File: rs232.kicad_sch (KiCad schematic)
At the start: 7 parts, among them U7 SP3223

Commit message: wen branch and pr
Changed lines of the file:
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@@
 		(company "Hoppen")
+	)
+	(bus_alias "RS232_IN"
+		(members "RS232_IN_T" "RS232_IN_R")
+	)
+	(bus_alias "VN_RS232"
+		(members "RS232_OUT_T" "RS232_OUT_R")
 	)
 	(rectangle
@@
 		)
 	)
-	(hierarchical_label "{RS232_OUT}"
+	(hierarchical_label "{VN_RS232}"
 		(shape input)
 		(at 182.88 107.95 0)

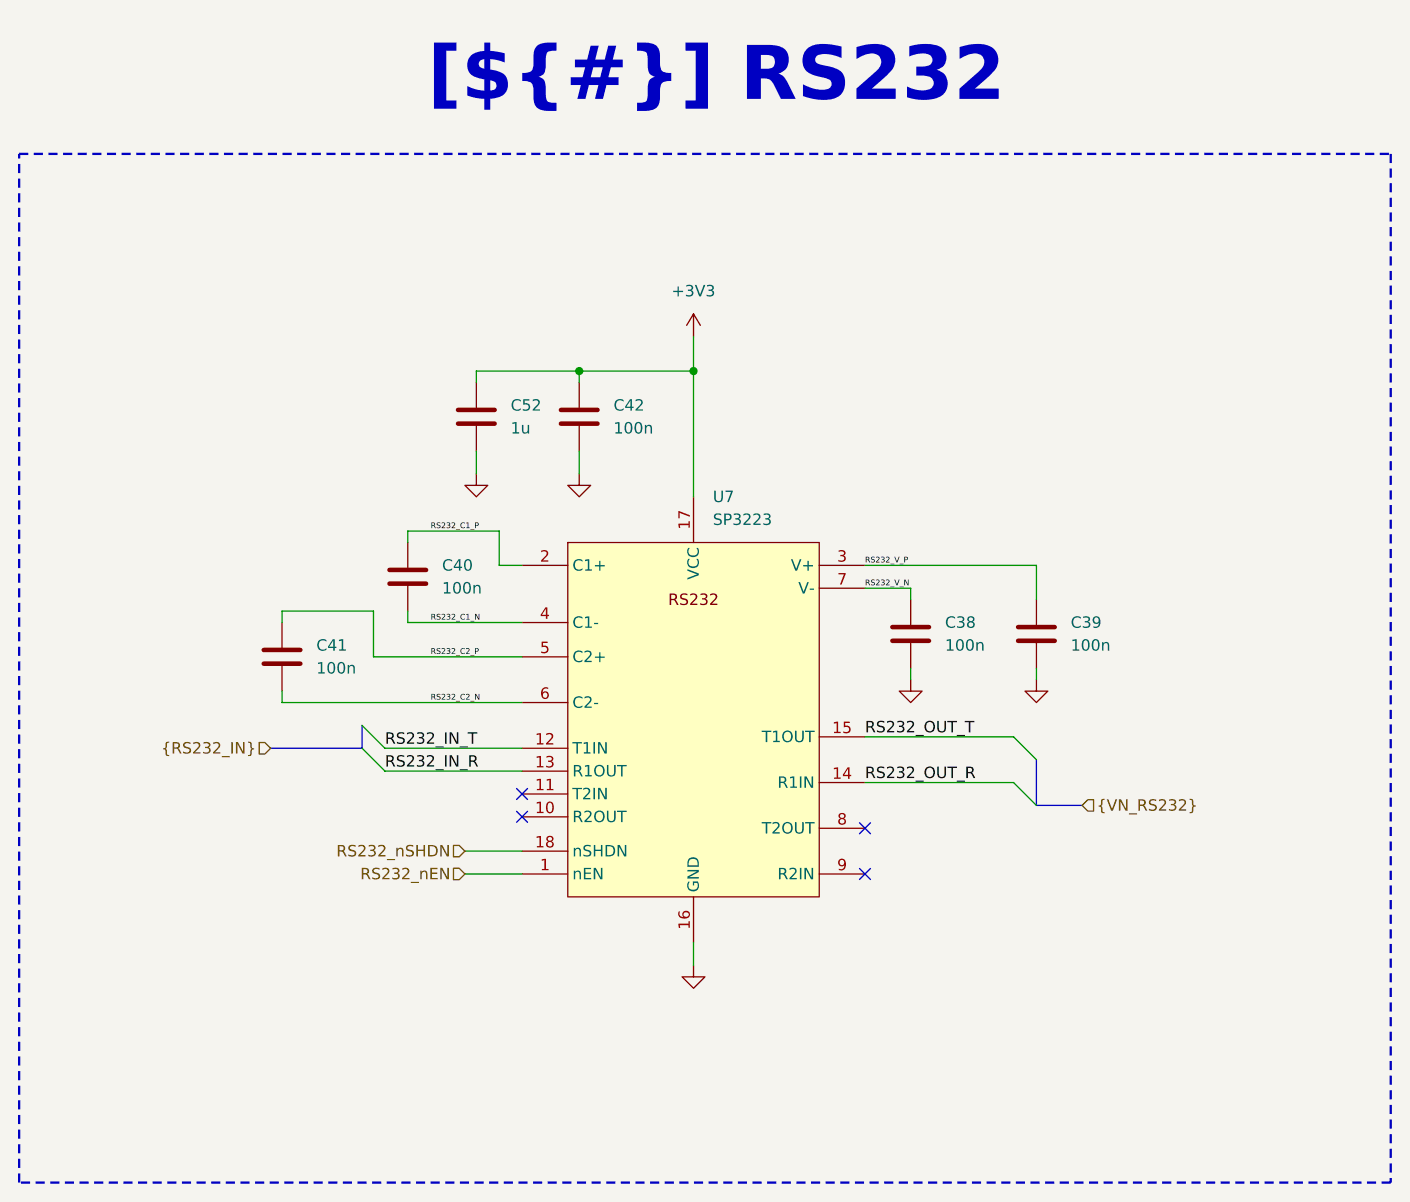
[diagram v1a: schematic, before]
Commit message: much work and .ioc file added
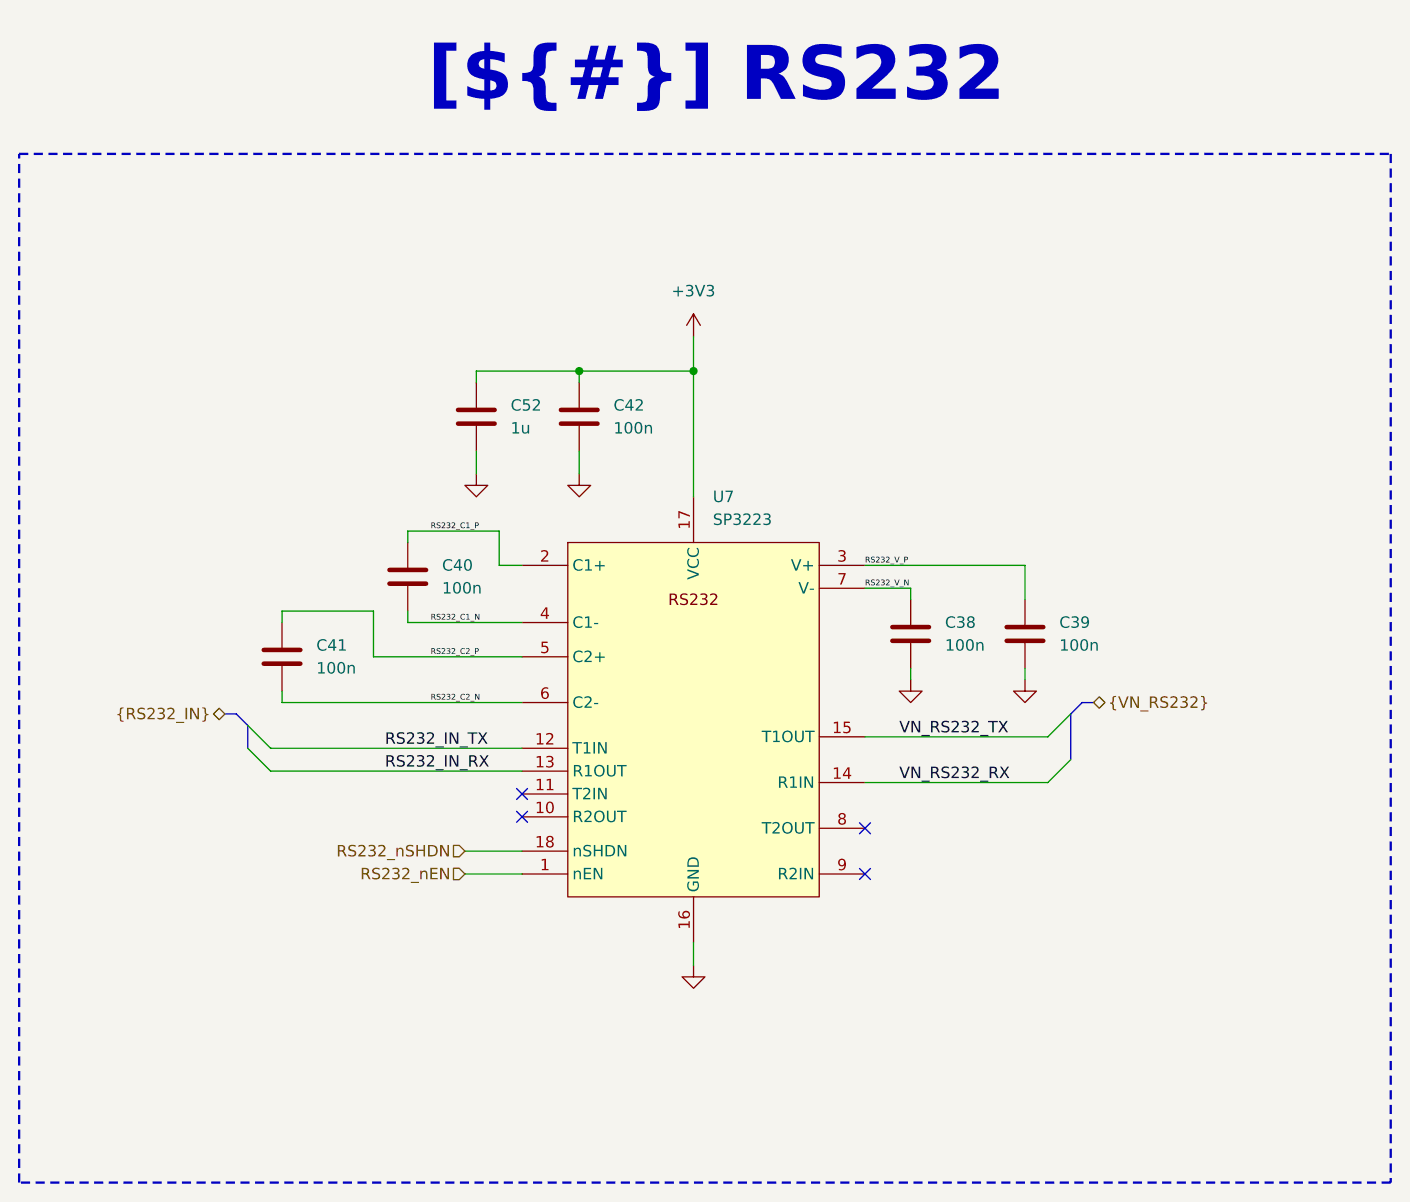
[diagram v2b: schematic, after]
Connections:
- net RS232_IN_R renamed RS232_IN_RX
- net RS232_IN_T renamed RS232_IN_TX
- net RS232_OUT_R renamed VN_RS232_RX
- net RS232_OUT_T renamed VN_RS232_TX
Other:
- moved on the sheet: C39

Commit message: start fix fp
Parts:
- C38, C39, C40, C41, C42: footprint (none) -> 0_capacitor_smd:C_0402_1005Metric
- U7: footprint (none) -> 0_transceivers:TSSOP-16_L5.0-W4.4-P0.65-LS6.4-BL
